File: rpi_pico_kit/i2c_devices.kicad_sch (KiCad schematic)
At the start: 11 parts, among them J7 Conn_01x04_Male, J8 OLED Display, J9 Conn_01x04_Male, U10 AT24CS32

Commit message: added another MPNs, edited color of LEDs
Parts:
- J7, J9: Manufacturer Part Number (none) -> PinHeader_1x04
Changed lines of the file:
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@@
+      (effects (font (size 1.27 1.27)) hide)
+    )
+    (property "Manufacturer Part Number" "PinHeader_1x04" (id 4) (at 140.97 78.74 0)
       (effects (font (size 1.27 1.27)) hide)
     )
@@
       (effects (font (size 1.27 1.27)) hide)
     )
+    (property "Manufacturer Part Number" "PinHeader_1x04" (id 4) (at 140.97 109.22 0)
+      (effects (font (size 1.27 1.27)) hide)
+    )

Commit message: added MPNs
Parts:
- J7, J9: Supplier (none) -> me
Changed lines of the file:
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@@
+      (effects (font (size 1.27 1.27)) hide)
+    )
+    (property "Supplier" "me" (id 5) (at 140.97 78.74 0)
       (effects (font (size 1.27 1.27)) hide)
     )
@@
       (effects (font (size 1.27 1.27)) hide)
     )
+    (property "Supplier" "me" (id 5) (at 140.97 109.22 0)
+      (effects (font (size 1.27 1.27)) hide)
+    )

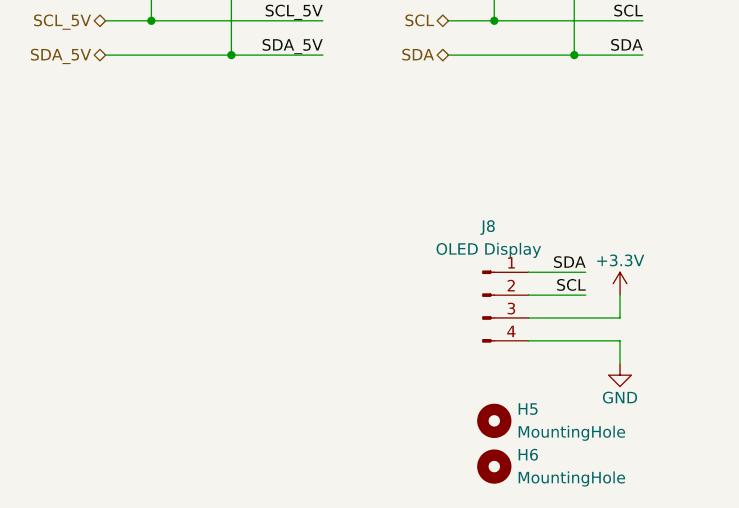
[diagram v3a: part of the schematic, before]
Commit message: added SSD1306 library
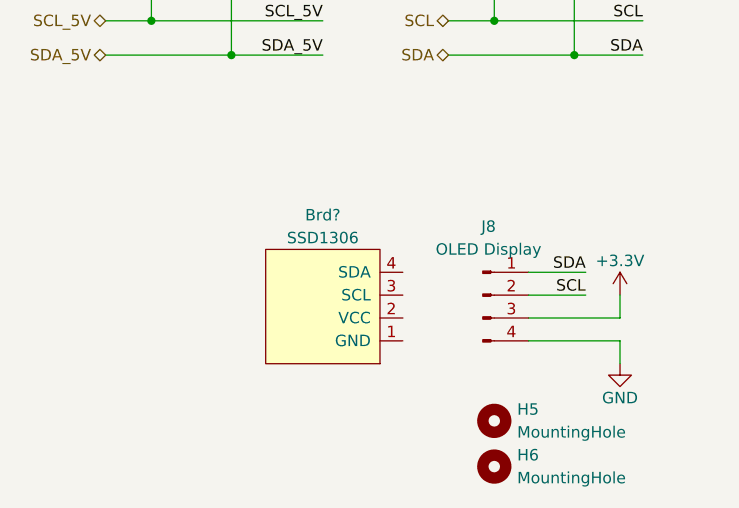
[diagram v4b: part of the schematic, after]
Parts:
- added Brd?: SSD1306, symbol SSD1306:SSD1306
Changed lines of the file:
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@@
     (pin "1")
+  )
+  (symbol (lib_id "SSD1306:SSD1306") (at 66.04 110.49 270) (mirror x) (unit 1)
+    (in_bom yes) (on_board yes) (fields_autoplaced)
+    (property "Reference" "Brd?" (id 0) (at 66.04 100.33 90)
+      (effects (font (size 1.27 1.27)))
+    )
+    (property "Value" "SSD1306" (id 1) (at 66.04 102.87 90)
+      (effects (font (size 1.27 1.27)))
+    )
+    (property "Footprint" "" (id 2) (at 72.39 110.49 0)
+      (effects (font (size 1.27 1.27)) hide)
+    )
+    (property "Datasheet" "" (id 3) (at 72.39 110.49 0)
+      (effects (font (size 1.27 1.27)) hide)
+    )
+    (pin "1")
+    (pin "2")
+    (pin "3")
+    (pin "4")
   )
   (symbol (lib_id "Memory_EEPROM:AT24CS32-SSHM") (at 209.55 99.06 0) (unit 1)

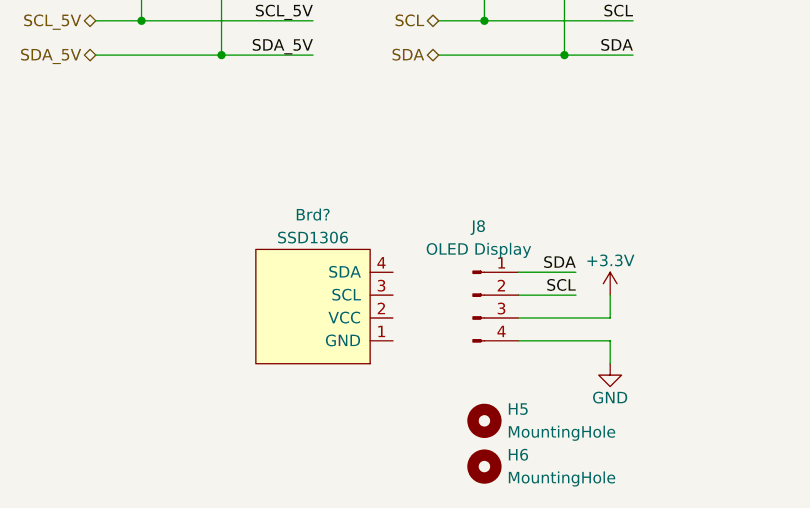
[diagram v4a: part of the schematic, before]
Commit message: migrated library SSD1306, added footprint
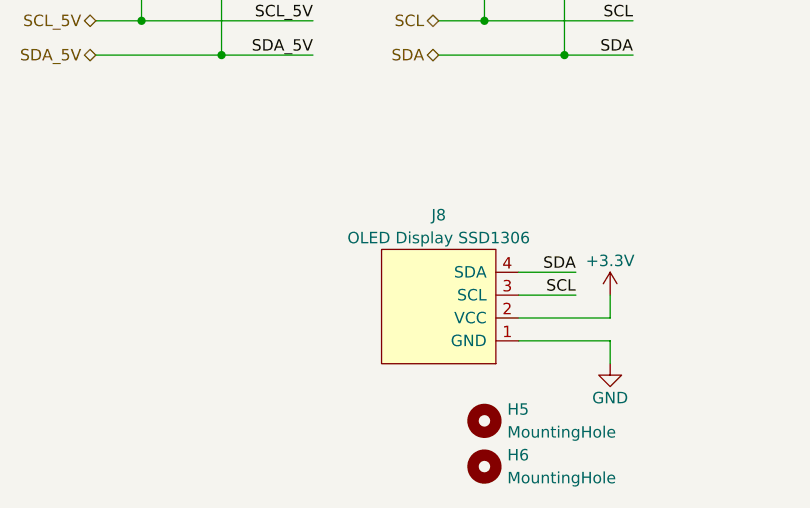
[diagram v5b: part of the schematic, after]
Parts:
- removed J8: OLED Display, symbol Connector:Conn_01x04_Male
- J8: renamed from Brd?; value SSD1306 -> OLED Display SSD1306; footprint (none) -> SSD1306:128x64OLED; Manufacturer Part Number (none) -> LA141008DI; Supplier (none) -> Laskakit; Supplier Part URL (none) -> https://www.laskakit.cz/oled-displej-modry-a-zluty-128x64-0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
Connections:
- net +3V3: now also J8.2 (VCC)
- net GND: now also J8.1 (GND)
- net SCL: now also J8.3 (SCL)
- net SDA: now also J8.4 (SDA)
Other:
- moved on the sheet: J8
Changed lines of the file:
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@@
     (pin "1")
-  )
-  (symbol (lib_id "Connector:Conn_01x04_Male") (at 83.82 109.22 0) (unit 1)
-    (in_bom yes) (on_board yes) (fields_autoplaced)
-    (property "Reference" "J8" (id 0) (at 84.455 101.6 0)
-      (effects (font (size 1.27 1.27)))
-    )
-    (property "Value" "OLED Display" (id 1) (at 84.455 104.14 0)
-      (effects (font (size 1.27 1.27)))
-    )
-    (property "Footprint" "" (id 2) (at 83.82 109.22 0)
-      (effects (font (size 1.27 1.27)) hide)
-    )
-    (property "Datasheet" "~" (id 3) (at 83.82 109.22 0)
-      (effects (font (size 1.27 1.27)) hide)
-    )
-    (property "Manufacturer Part Number" "LA141008DI" (id 4) (at 83.82 109.22 0)
-      (effects (font (size 1.27 1.27)) hide)
-    )
-    (property "Supplier" "Laskakit" (id 5) (at 83.82 109.22 0)
-      (effects (font (size 1.27 1.27)) hide)
-    )
-    (property "Supplier Part URL" "https://www.laskakit.cz/oled-displej-modry-a-zluty-128x64-0-96--i2c/" (id 6) (at 83.82 109.22 0)
-      (effects (font (size 1.27 1.27)) hide)
-    )
-    (pin "1")
-    (pin "2")
-    (pin "3")
-    (pin "4")
   )
   (symbol (lib_id "power:+3.3V") (at 93.98 66.04 0) (unit 1)
@@
     (pin "1")
   )
-  (symbol (lib_id "SSD1306:SSD1306") (at 66.04 110.49 270) (mirror x) (unit 1)
+  (symbol (lib_id "SSD1306:SSD1306") (at 80.01 110.49 270) (mirror x) (unit 1)
     (in_bom yes) (on_board yes) (fields_autoplaced)
-    (property "Reference" "Brd?" (id 0) (at 66.04 100.33 90)
+    (property "Reference" "J8" (id 0) (at 80.01 100.33 90)
       (effects (font (size 1.27 1.27)))
     )
-    (property "Value" "SSD1306" (id 1) (at 66.04 102.87 90)
+    (property "Value" "OLED Display SSD1306" (id 1) (at 80.01 102.87 90)
       (effects (font (size 1.27 1.27)))
     )
-    (property "Footprint" "" (id 2) (at 72.39 110.49 0)
+    (property "Footprint" "SSD1306:128x64OLED" (id 2) (at 86.36 110.49 0)
       (effects (font (size 1.27 1.27)) hide)
     )
-    (property "Datasheet" "" (id 3) (at 72.39 110.49 0)
+    (property "Datasheet" "" (id 3) (at 86.36 110.49 0)
       (effects (font (size 1.27 1.27)) hide)
     )
+    (property "Manufacturer Part Number" "LA141008DI" (id 4) (at 80.01 110.49 0)
+      (effects (font (size 1.27 1.27)) hide)
+    )
+    (property "Supplier" "Laskakit" (id 5) (at 80.01 110.49 0)
+      (effects (font (size 1.27 1.27)) hide)
+    )
+    (property "Supplier Part URL" "https://www.laskakit.cz/oled-displej-modry-a-zluty-128x64-0-96--i2c/" (id 6) (at 80.01 110.49 0)
+      (effects (font (size 1.27 1.27)) hide)
+    )

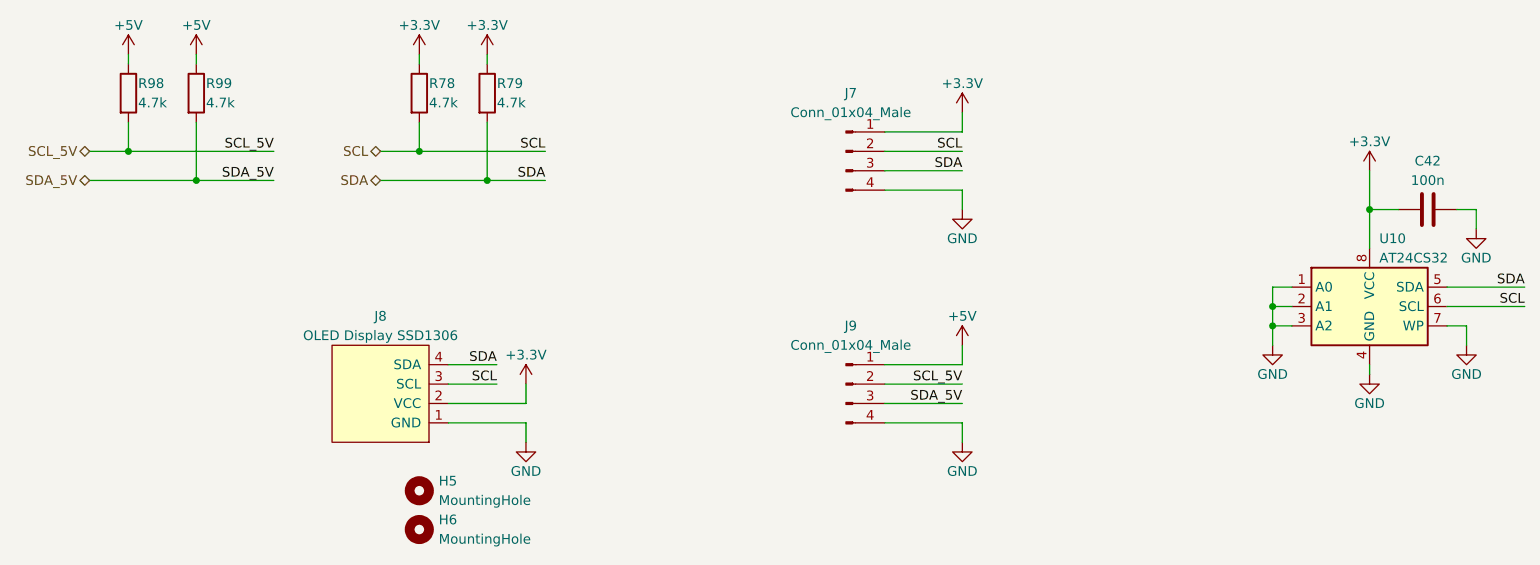
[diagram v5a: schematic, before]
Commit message: changed numbering of parts
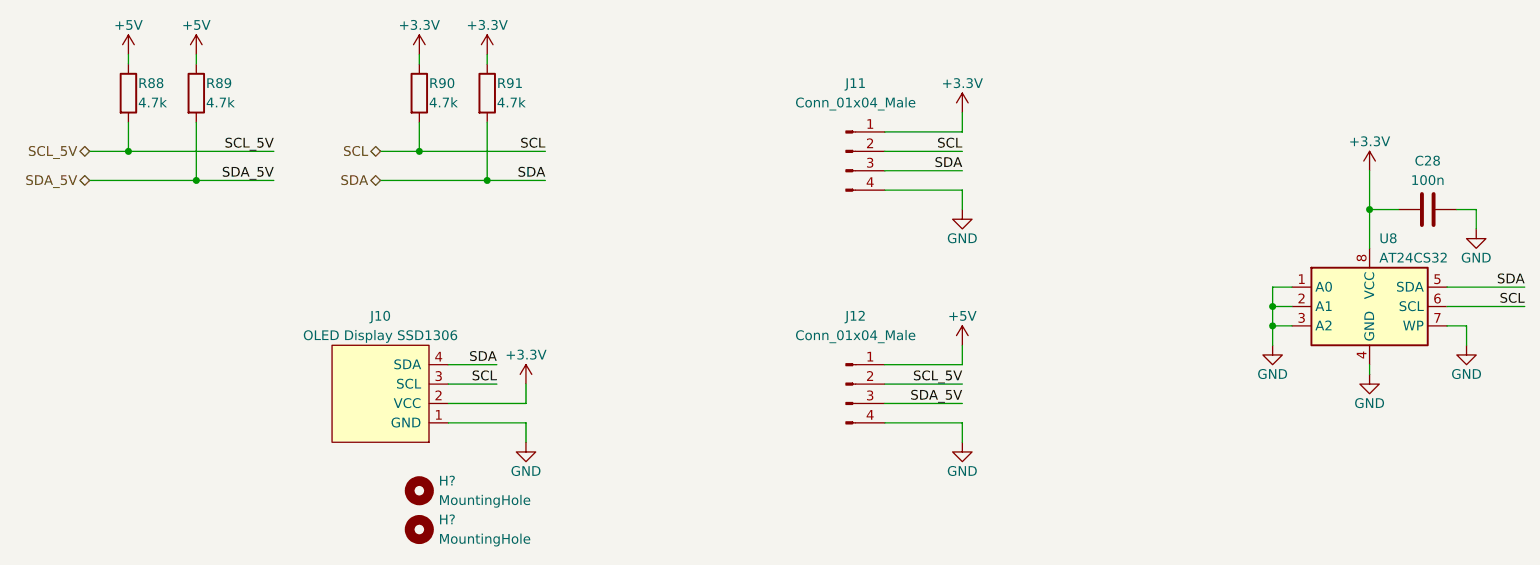
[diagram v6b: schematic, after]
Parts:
- renumbered C42 to C28, H6 to H?, H5 to H?, J8 to J10, J7 to J11, J9 to J12, R98 to R88, R99 to R89, R78 to R90, R79 to R91, U10 to U8
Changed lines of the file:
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@@
   (symbol (lib_id "Mechanical:MountingHole") (at 85.09 128.27 0) (unit 1)
     (in_bom yes) (on_board yes) (fields_autoplaced)
-    (property "Reference" "H6" (id 0) (at 87.63 126.9999 0)
+    (property "Reference" "H?" (id 0) (at 87.63 126.9999 0)
       (effects (font (size 1.27 1.27)) (justify left))
     )
@@
   (symbol (lib_id "Device:C") (at 217.17 86.36 90) (unit 1)
     (in_bom yes) (on_board yes)
-    (property "Reference" "C42" (id 0) (at 217.17 80.01 90)
+    (property "Reference" "C28" (id 0) (at 217.17 80.01 90)
       (effects (font (size 1.27 1.27)))
     )
@@
   (symbol (lib_id "power:GND") (at 156.21 116.84 0) (unit 1)
     (in_bom yes) (on_board yes)
-    (property "Reference" "#PWR0104" (id 0) (at 156.21 123.19 0)
+    (property "Reference" "#PWR?" (id 0) (at 156.21 123.19 0)
       (effects (font (size 1.27 1.27)) hide)
     )
@@
   (symbol (lib_id "power:+3.3V") (at 156.21 73.66 0) (unit 1)
     (in_bom yes) (on_board yes)
-    (property "Reference" "#PWR0101" (id 0) (at 156.21 77.47 0)
+    (property "Reference" "#PWR?" (id 0) (at 156.21 77.47 0)
       (effects (font (size 1.27 1.27)) hide)
     )
@@
   (symbol (lib_id "Device:R") (at 93.98 71.12 0) (unit 1)
     (in_bom yes) (on_board yes)
-    (property "Reference" "R79" (id 0) (at 95.25 69.85 0)
+    (property "Reference" "R91" (id 0) (at 95.25 69.85 0)
       (effects (font (size 1.27 1.27)) (justify left))
     )
@@
   (symbol (lib_id "Device:R") (at 46.99 71.12 0) (unit 1)
     (in_bom yes) (on_board yes)
-    (property "Reference" "R98" (id 0) (at 48.26 69.85 0)
+    (property "Reference" "R88" (id 0) (at 48.26 69.85 0)
       (effects (font (size 1.27 1.27)) (justify left))
     )
@@
   (symbol (lib_id "power:GND") (at 156.21 86.36 0) (unit 1)
     (in_bom yes) (on_board yes)
-    (property "Reference" "#PWR0102" (id 0) (at 156.21 92.71 0)
+    (property "Reference" "#PWR?" (id 0) (at 156.21 92.71 0)
       (effects (font (size 1.27 1.27)) hide)
     )
@@
   (symbol (lib_id "power:GND") (at 99.06 116.84 0) (unit 1)
     (in_bom yes) (on_board yes)
-    (property "Reference" "#PWR0106" (id 0) (at 99.06 123.19 0)
+    (property "Reference" "#PWR?" (id 0) (at 99.06 123.19 0)
       (effects (font (size 1.27 1.27)) hide)
     )
@@
   (symbol (lib_id "power:GND") (at 222.25 104.14 0) (unit 1)
     (in_bom yes) (on_board yes)
-    (property "Reference" "#PWR0144" (id 0) (at 222.25 110.49 0)
+    (property "Reference" "#PWR?" (id 0) (at 222.25 110.49 0)
       (effects (font (size 1.27 1.27)) hide)
     )
@@
   (symbol (lib_id "power:+5V") (at 46.99 66.04 0) (unit 1)
     (in_bom yes) (on_board yes)
-    (property "Reference" "#PWR0161" (id 0) (at 46.99 69.85 0)
+    (property "Reference" "#PWR?" (id 0) (at 46.99 69.85 0)
       (effects (font (size 1.27 1.27)) hide)
     )
@@
   (symbol (lib_id "power:+3.3V") (at 85.09 66.04 0) (unit 1)
     (in_bom yes) (on_board yes)
-    (property "Reference" "#PWR099" (id 0) (at 85.09 69.85 0)
+    (property "Reference" "#PWR?" (id 0) (at 85.09 69.85 0)
       (effects (font (size 1.27 1.27)) hide)
     )
@@
   (symbol (lib_id "power:+3.3V") (at 93.98 66.04 0) (unit 1)
     (in_bom yes) (on_board yes)
-    (property "Reference" "#PWR0100" (id 0) (at 93.98 69.85 0)
+    (property "Reference" "#PWR?" (id 0) (at 93.98 69.85 0)
       (effects (font (size 1.27 1.27)) hide)
     )
@@
   (symbol (lib_id "SSD1306:SSD1306") (at 80.01 110.49 270) (mirror x) (unit 1)
     (in_bom yes) (on_board yes) (fields_autoplaced)
-    (property "Reference" "J8" (id 0) (at 80.01 100.33 90)
+    (property "Reference" "J10" (id 0) (at 80.01 100.33 90)
       (effects (font (size 1.27 1.27)))
     )
@@
       (effects (font (size 1.27 1.27)) hide)
     )
-    (property "Datasheet" "" (id 3) (at 86.36 110.49 0)
+    (property "Datasheet" "~" (id 3) (at 86.36 110.49 0)
       (effects (font (size 1.27 1.27)) hide)
     )
@@
   (symbol (lib_id "Memory_EEPROM:AT24CS32-SSHM") (at 209.55 99.06 0) (unit 1)
     (in_bom yes) (on_board yes)
-    (property "Reference" "U10" (id 0) (at 210.82 90.17 0)
+    (property "Reference" "U8" (id 0) (at 210.82 90.17 0)
       (effects (font (size 1.27 1.27)) (justify left))
     )
@@
   )
   (symbol (lib_id "Connector:Conn_01x04_Male") (at 140.97 78.74 0) (unit 1)
-    (in_bom yes) (on_board yes) (fields_autoplaced)
-    (property "Reference" "J7" (id 0) (at 141.605 71.12 0)
-      (effects (font (size 1.27 1.27)))
-    )
-    (property "Value" "Conn_01x04_Male" (id 1) (at 141.605 73.66 0)
+    (in_bom yes) (on_board yes)
+    (property "Reference" "J11" (id 0) (at 142.24 69.85 0)
+      (effects (font (size 1.27 1.27)))
+    )
+    (property "Value" "Conn_01x04_Male" (id 1) (at 142.24 72.39 0)
       (effects (font (size 1.27 1.27)))
     )
@@
   (symbol (lib_id "power:+5V") (at 55.88 66.04 0) (unit 1)
     (in_bom yes) (on_board yes)
-    (property "Reference" "#PWR0162" (id 0) (at 55.88 69.85 0)
+    (property "Reference" "#PWR?" (id 0) (at 55.88 69.85 0)
       (effects (font (size 1.27 1.27)) hide)
     )
@@
   )
   (symbol (lib_id "Connector:Conn_01x04_Male") (at 140.97 109.22 0) (unit 1)
-    (in_bom yes) (on_board yes) (fields_autoplaced)
-    (property "Reference" "J9" (id 0) (at 141.605 101.6 0)
-      (effects (font (size 1.27 1.27)))
-    )
-    (property "Value" "Conn_01x04_Male" (id 1) (at 141.605 104.14 0)
+    (in_bom yes) (on_board yes)
+    (property "Reference" "J12" (id 0) (at 142.24 100.33 0)
+      (effects (font (size 1.27 1.27)))
+    )
+    (property "Value" "Conn_01x04_Male" (id 1) (at 142.24 102.87 0)
       (effects (font (size 1.27 1.27)))
     )
@@
   (symbol (lib_id "power:+3.3V") (at 99.06 109.22 0) (unit 1)
     (in_bom yes) (on_board yes)
-    (property "Reference" "#PWR0105" (id 0) (at 99.06 113.03 0)
+    (property "Reference" "#PWR?" (id 0) (at 99.06 113.03 0)
       (effects (font (size 1.27 1.27)) hide)
     )
@@
   (symbol (lib_id "Device:R") (at 85.09 71.12 0) (unit 1)
     (in_bom yes) (on_board yes)
-    (property "Reference" "R78" (id 0) (at 86.36 69.85 0)
+    (property "Reference" "R90" (id 0) (at 86.36 69.85 0)
       (effects (font (size 1.27 1.27)) (justify left))
     )
@@
   (symbol (lib_id "power:GND") (at 209.55 107.95 0) (unit 1)
     (in_bom yes) (on_board yes)
-    (property "Reference" "#PWR0143" (id 0) (at 209.55 114.3 0)
+    (property "Reference" "#PWR?" (id 0) (at 209.55 114.3 0)
       (effects (font (size 1.27 1.27)) hide)
     )
@@
   (symbol (lib_id "power:+5V") (at 156.21 104.14 0) (unit 1)
     (in_bom yes) (on_board yes)
-    (property "Reference" "#PWR0103" (id 0) (at 156.21 107.95 0)
+    (property "Reference" "#PWR?" (id 0) (at 156.21 107.95 0)
       (effects (font (size 1.27 1.27)) hide)
     )
@@
   (symbol (lib_id "Device:R") (at 55.88 71.12 0) (unit 1)
     (in_bom yes) (on_board yes)
-    (property "Reference" "R99" (id 0) (at 57.15 69.85 0)
+    (property "Reference" "R89" (id 0) (at 57.15 69.85 0)
       (effects (font (size 1.27 1.27)) (justify left))
     )
@@
   (symbol (lib_id "power:GND") (at 196.85 104.14 0) (unit 1)
     (in_bom yes) (on_board yes)
-    (property "Reference" "#PWR0141" (id 0) (at 196.85 110.49 0)
+    (property "Reference" "#PWR?" (id 0) (at 196.85 110.49 0)
       (effects (font (size 1.27 1.27)) hide)
     )
@@
   (symbol (lib_id "power:+3.3V") (at 209.55 81.28 0) (unit 1)
     (in_bom yes) (on_board yes)
-    (property "Reference" "#PWR0142" (id 0) (at 209.55 85.09 0)
+    (property "Reference" "#PWR?" (id 0) (at 209.55 85.09 0)
       (effects (font (size 1.27 1.27)) hide)
     )
@@
   (symbol (lib_id "power:GND") (at 223.52 88.9 0) (unit 1)
     (in_bom yes) (on_board yes)
-    (property "Reference" "#PWR0145" (id 0) (at 223.52 95.25 0)
+    (property "Reference" "#PWR?" (id 0) (at 223.52 95.25 0)
       (effects (font (size 1.27 1.27)) hide)
     )
@@
   (symbol (lib_id "Mechanical:MountingHole") (at 85.09 123.19 0) (unit 1)
     (in_bom yes) (on_board yes) (fields_autoplaced)
-    (property "Reference" "H5" (id 0) (at 87.63 121.9199 0)
-      (effects (font (size 1.27 1.27)) (justify left))
-    )
+    (property "Reference" "H?" (id 0) (at 87.63 121.9199 0)
+      (effects (font (size 1.27 1.27)) (justify left))
+    )
